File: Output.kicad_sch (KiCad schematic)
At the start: 46 parts, among them J20 Conn_01x02, J21 Conn_01x02, Q1 2N7002NXAK, Q10 2N7002NXAK, Q11 2N7002NXAK, Q2 NTR5105PT1G, Q3 NTR5105PT1G, Q4 2N7002NXAK, Q5 2N7002NXAK, Q6 2N7002NXAK, Q7 2N7002NXAK, Q8 2N7002NXAK, Q9 2N7002NXAK

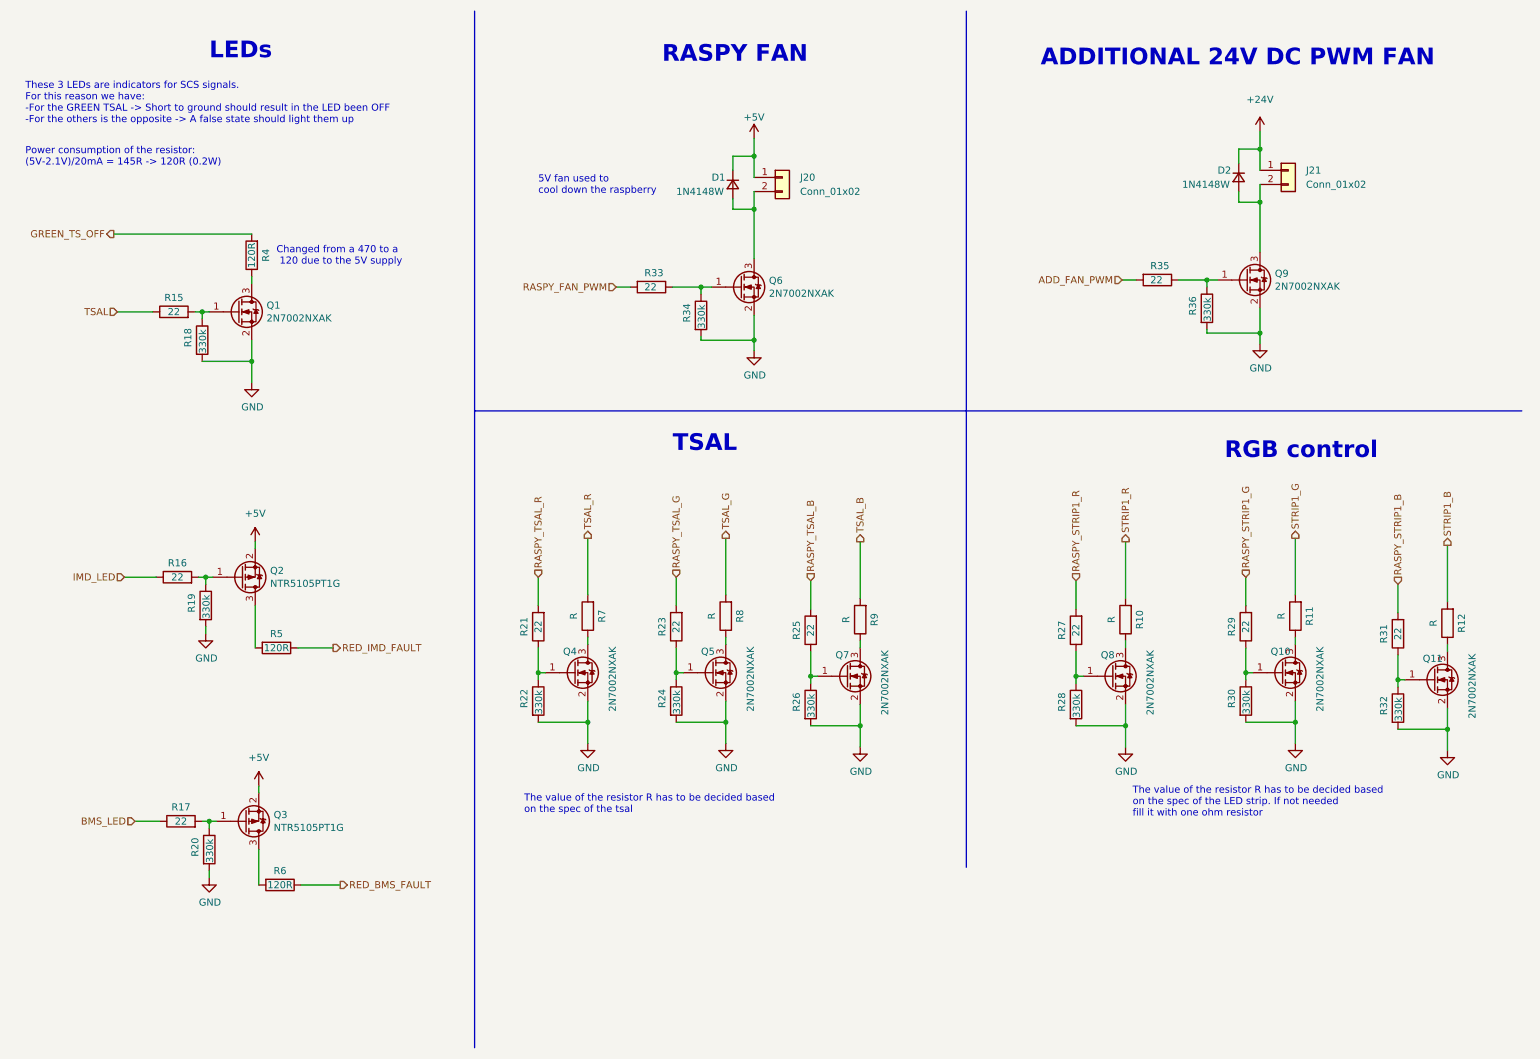
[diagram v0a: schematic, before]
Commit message: Changed mosfet, fixed all the datasheets, added 3D models
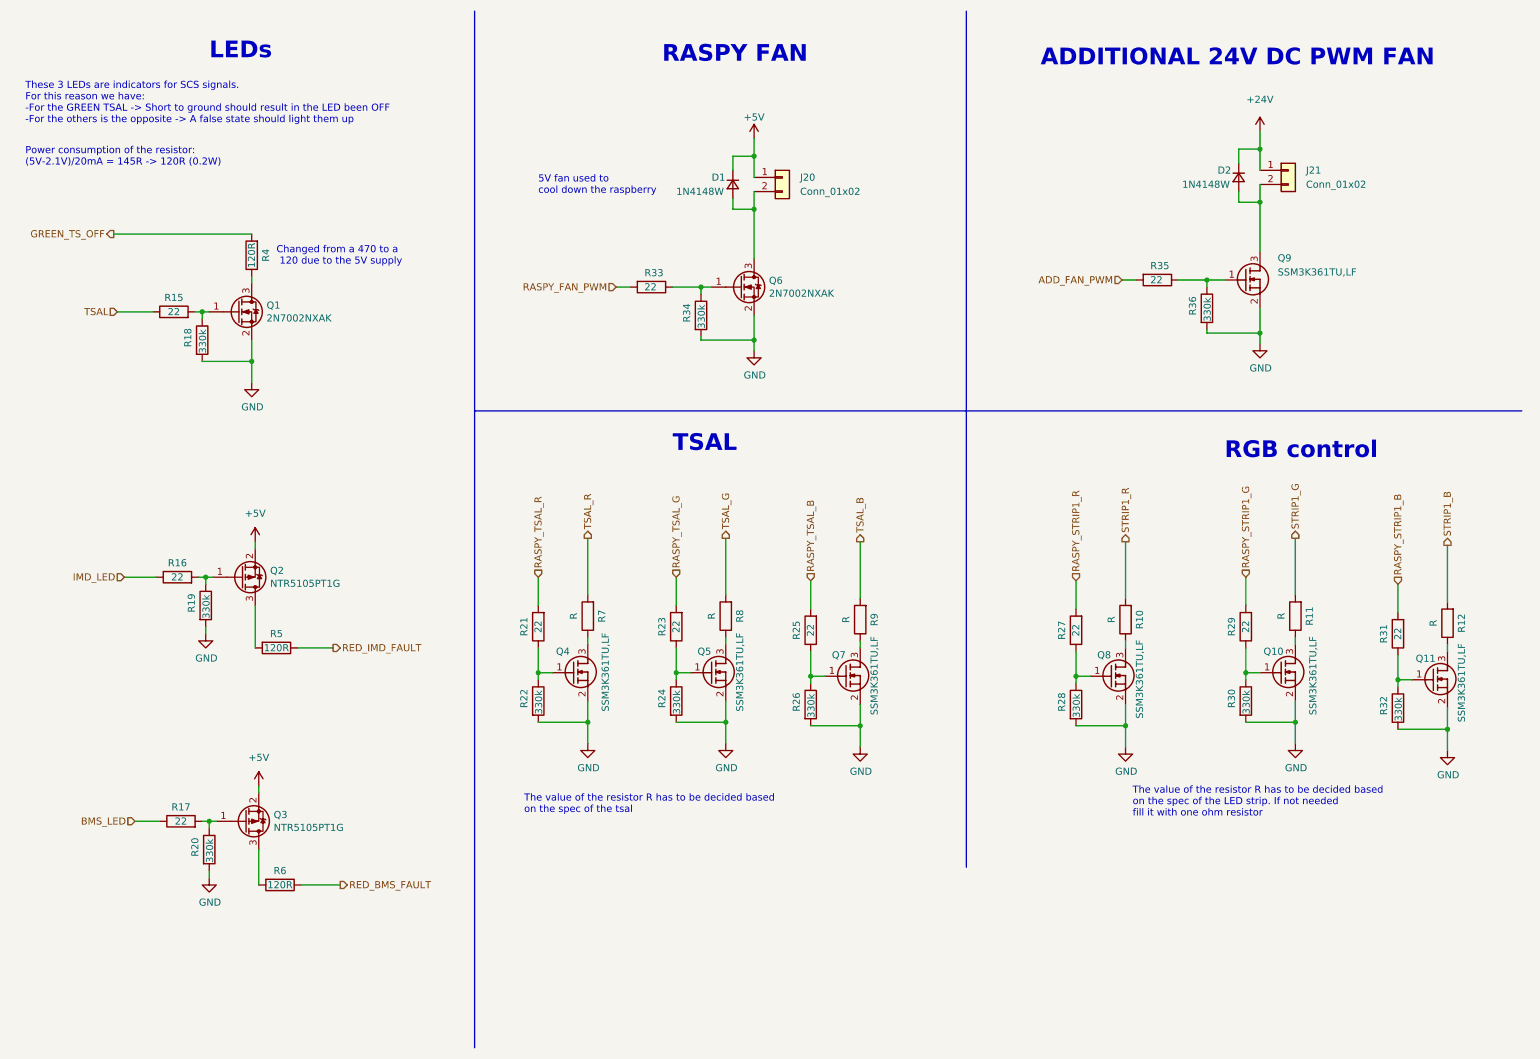
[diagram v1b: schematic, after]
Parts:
- removed Q10, Q11, Q4, Q5, Q7, Q8, Q9: 2N7002NXAK, Package_TO_SOT_SMD:SOT-23, symbol Device:Q_NMOS_GSD
- added Q10, Q11, Q4, Q5, Q7, Q8, Q9: SSM3K361TU,LF, 00_proj-lib:SOTFL65P210X75-3N, symbol 00_proj-lib:SSM3K361TU,LF
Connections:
- net GND: now also Q10.2 (S), Q11.2 (S), Q4.2 (S), Q5.2 (S), Q7.2 (S), Q8.2 (S), Q9.2 (S)
- net at R27.1, R28.1: now also Q8.1 (G)
- net at R10.1: now also Q8.3 (D)
- net at R23.1, R24.1: now also Q5.1 (G)
- net at D2.2 (A), J21.2 (Pin_2): now also Q9.3 (D)
- net at R12.1: now also Q11.3 (D)
- net at R11.1: now also Q10.3 (D)
- net at R31.1, R32.1: now also Q11.1 (G)
- net at R25.1, R26.1: now also Q7.1 (G)
- net at R35.1, R36.1: now also Q9.1 (G)
- net at R8.1: now also Q5.3 (D)
- net at R9.1: now also Q7.3 (D)
- net at R29.1, R30.1: now also Q10.1 (G)
- net at R21.1, R22.1: now also Q4.1 (G)
- net at R7.1: now also Q4.3 (D)

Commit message: Major changes after the schematic review. Refer to Github for all the changes
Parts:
- removed D1, D2: 1N4148W, Diode_SMD:D_SOD-323_HandSoldering, symbol Device:D_Small
- removed J20: Conn_01x02, Connector_Molex:Molex_Micro-Fit_3.0_43650-0215_1x02_P3.00mm_Vertical, symbol Connector_Generic:Conn_01x02
- removed Q6: 2N7002NXAK, Package_TO_SOT_SMD:SOT-23, symbol Device:Q_NMOS_GSD
- removed Q9: SSM3K361TU,LF, 00_proj-lib:SOTFL65P210X75-3N, symbol 00_proj-lib:SSM3K361TU,LF
- removed R33, R35: 22, Resistor_SMD:R_0603_1608Metric, symbol Device:R
- removed R34, R36: 330k, Resistor_SMD:R_0603_1608Metric, symbol Device:R
- added J22: RED_IMD_FAULT, Connector_Molex:Molex_Micro-Fit_3.0_43650-0215_1x02_P3.00mm_Vertical, symbol Connector_Generic:Conn_01x02
- added J23: RED_BMS_FAULT, Connector_Molex:Molex_Micro-Fit_3.0_43650-0215_1x02_P3.00mm_Vertical, symbol Connector_Generic:Conn_01x02
- added J24: RGB_STRIP, Connector_Molex:Molex_Micro-Fit_3.0_43650-0400_1x04_P3.00mm_Horizontal, symbol Connector_Generic:Conn_01x04
- added J25: TSAL, Connector_Molex:Molex_Micro-Fit_3.0_43650-0400_1x04_P3.00mm_Horizontal, symbol Connector_Generic:Conn_01x04
- added J?: ADD_RGB_STRIP, Connector_Molex:Molex_Micro-Fit_3.0_43650-0315_1x03_P3.00mm_Vertical, symbol Connector_Generic:Conn_01x03
- added JP?: 5V_ADD_STRIP, symbol Jumper:SolderJumper_2_Open
- added JP?: 3V3_ADD_STRIP, symbol Jumper:SolderJumper_2_Open
- J21: value Conn_01x02 -> GREEN_TS_OFF
- Q10: renamed from Q7; symbol 00_proj-lib:SSM3K361TU,LF -> Device:Q_NMOS_GSD
- Q11: symbol 00_proj-lib:SSM3K361TU,LF -> Device:Q_NMOS_GSD
- Q6: renamed from Q4; symbol 00_proj-lib:SSM3K361TU,LF -> Device:Q_NMOS_GSD
- Q7: renamed from Q8; symbol 00_proj-lib:SSM3K361TU,LF -> Device:Q_NMOS_GSD
- Q8: renamed from Q10; symbol 00_proj-lib:SSM3K361TU,LF -> Device:Q_NMOS_GSD
- Q9: renamed from Q5; symbol 00_proj-lib:SSM3K361TU,LF -> Device:Q_NMOS_GSD
- R10: renamed from R16; value 22 -> 22R
- R11: renamed from R17; value 22 -> 22R
- R15: renamed from R4; footprint Resistor_SMD:R_2512_6332Metric -> Resistor_SMD:R_0603_1608Metric
- R16: renamed from R5; footprint Resistor_SMD:R_2512_6332Metric -> Resistor_SMD:R_0603_1608Metric
- R17: renamed from R6; footprint Resistor_SMD:R_2512_6332Metric -> Resistor_SMD:R_0603_1608Metric
- R18: renamed from R21; value 22 -> 22R
- R19: renamed from R27; value 22 -> 22R
- R22: renamed from R7; footprint Resistor_SMD:R_1206_3216Metric -> Resistor_SMD:R_0805_2012Metric
- R23: renamed from R10; footprint Resistor_SMD:R_1206_3216Metric -> Resistor_SMD:R_0805_2012Metric
- R24: renamed from R23; value 22 -> 22R
- R25: renamed from R29; value 22 -> 22R
- R28: renamed from R11; footprint Resistor_SMD:R_1206_3216Metric -> Resistor_SMD:R_0805_2012Metric
- R29: renamed from R8; footprint Resistor_SMD:R_1206_3216Metric -> Resistor_SMD:R_0805_2012Metric
- R30: renamed from R25; value 22 -> 22R
- R31: value 22 -> 22R
- R34: renamed from R9; footprint Resistor_SMD:R_1206_3216Metric -> Resistor_SMD:R_0805_2012Metric
- R35: renamed from R12; footprint Resistor_SMD:R_1206_3216Metric -> Resistor_SMD:R_0805_2012Metric
- R9: renamed from R15; value 22 -> 22R
- renumbered Q1 to Q3, Q2 to Q4, Q3 to Q5, R18 to R12, R19 to R13, R20 to R14, R22 to R20, R28 to R21, R24 to R26, R30 to R27, R26 to R32, R32 to R33
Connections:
- net GREEN_TS_OFF is gone; now on an unnamed net: R15.2
- net RED_BMS_FAULT is gone; now on an unnamed net: R17.1
- net RED_IMD_FAULT is gone; now on an unnamed net: R16.1
- net +24V: now also J25.1 (Pin_1); no longer J21.1 (Pin_1)
- net +5V: now also J21.1 (Pin_1), JP?.2 (B)
- net GND: now also J22.2 (Pin_2), J23.2 (Pin_2), J?.3 (Pin_3)
- net STRIP1_B: now also J24.4 (Pin_4)
- net STRIP1_G: now also J24.3 (Pin_3)
- net STRIP1_R: now also J24.2 (Pin_2)
- net TSAL_B: now also J25.4 (Pin_4)
- net TSAL_G: now also J25.3 (Pin_3)
- net TSAL_R: now also J25.2 (Pin_2)
- net at Q5.3 (D): no longer R17.2
- net at Q4.3 (D): no longer R16.2
- new net: J?.1 (Pin_1), JP?.1 (A), JP?.1 (A)
- new net: J23.1 (Pin_1), R17.2
- new net: J22.1 (Pin_1), R16.2
- new net +12V: J24.1 (Pin_1)
- new net +3V3: JP?.2 (B)
- new net ADD_RGB_STRIP: J?.2 (Pin_2)
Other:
- note added: "ADDRESSABLE LED STRIP"
- note added: "The strip have to use the WS2812 interface in order to be controlled by the raspberry"
- note removed: "5V fan used to cool down the raspberry"
- note removed: "ADDITIONAL 24V DC PWM FAN"
- note removed: "Changed from a 470 to a 120 due to the 5V supply"
- note removed: "RASPY FAN"
- moved on the sheet: Q3, Q4, Q5, R10, R11, R12, R13, R14, R15, R16, R17, R18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

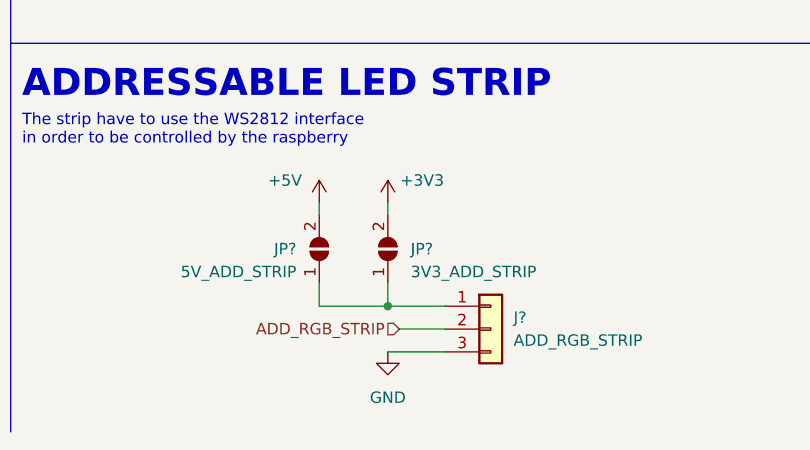
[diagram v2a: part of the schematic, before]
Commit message: modified schematic and started design pcb
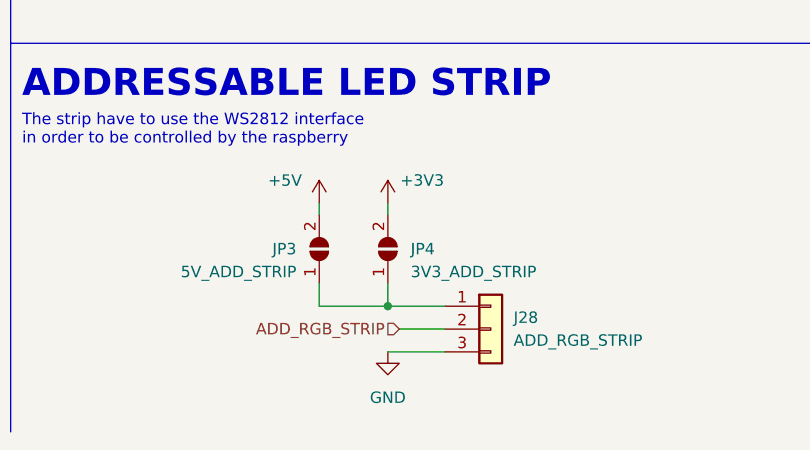
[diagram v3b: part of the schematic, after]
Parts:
- J21, J22, J23: footprint Connector_Molex:Molex_Micro-Fit_3.0_43650-0215_1x02_P3.00mm_Vertical -> Connector_Molex:Molex_Micro-Fit_3.0_43650-0200_1x02_P3.00mm_Horizontal
- JP3, JP4: renamed from JP?; footprint (none) -> Jumper:SolderJumper-2_P1.3mm_Open_RoundedPad1.0x1.5mm
- gave numbers to parts that had none: 1
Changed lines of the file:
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@@
   (symbol (lib_id "power:+5V") (at 113.03 171.45 0) (unit 1)
     (in_bom yes) (on_board yes)
-    (property "Reference" "#PWR?" (id 0) (at 113.03 175.26 0)
+    (property "Reference" "#PWR0129" (id 0) (at 113.03 175.26 0)
       (effects (font (size 1.27 1.27)) hide)
     )
@@
   (symbol (lib_id "Jumper:SolderJumper_2_Open") (at 113.03 176.53 270) (mirror x) (unit 1)
     (in_bom yes) (on_board yes)
-    (property "Reference" "JP?" (id 0) (at 110.49 176.53 90)
+    (property "Reference" "JP3" (id 0) (at 110.49 176.53 90)
       (effects (font (size 1.27 1.27)) (justify right))
     )
@@
       (effects (font (size 1.27 1.27)) (justify right))
     )
-    (property "Footprint" "" (id 2) (at 113.03 176.53 0)
+    (property "Footprint" "Jumper:SolderJumper-2_P1.3mm_Open_RoundedPad1.0x1.5mm" (id 2) (at 113.03 176.53 0)
       (effects (font (size 1.27 1.27)) hide)
     )
@@
   (symbol (lib_id "power:GND") (at 120.65 187.96 0) (unit 1)
     (in_bom yes) (on_board yes) (fields_autoplaced)
-    (property "Reference" "#PWR?" (id 0) (at 120.65 194.31 0)
+    (property "Reference" "#PWR0128" (id 0) (at 120.65 194.31 0)
       (effects (font (size 1.27 1.27)) hide)
     )
@@
   (symbol (lib_id "power:+3V3") (at 120.65 171.45 0) (unit 1)
     (in_bom yes) (on_board yes)
-    (property "Reference" "#PWR?" (id 0) (at 120.65 175.26 0)
+    (property "Reference" "#PWR0130" (id 0) (at 120.65 175.26 0)
       (effects (font (size 1.27 1.27)) hide)
     )
@@
   (symbol (lib_id "Connector_Generic:Conn_01x03") (at 132.08 185.42 0) (unit 1)
     (in_bom yes) (on_board yes) (fields_autoplaced)
-    (property "Reference" "J?" (id 0) (at 134.62 184.1499 0)
+    (property "Reference" "J28" (id 0) (at 134.62 184.1499 0)
       (effects (font (size 1.27 1.27)) (justify left))
     )
@@
     (property "Reference" "J21" (id 0) (at 67.31 48.26 0))
     (property "Value" "GREEN_TS_OFF" (id 1) (at 67.31 50.8 0))
-    (property "Footprint" "Connector_Molex:Molex_Micro-Fit_3.0_43650-0215_1x02_P3.00mm_Vertical" (id 2) (at 58.42 49.53 0)
+    (property "Footprint" "Connector_Molex:Molex_Micro-Fit_3.0_43650-0200_1x02_P3.00mm_Horizontal" (id 2) (at 58.42 49.53 0)
       (effects (font (size 1.27 1.27)) hide)
     )
@@
   (symbol (lib_id "Jumper:SolderJumper_2_Open") (at 120.65 176.53 90) (unit 1)
     (in_bom yes) (on_board yes)
-    (property "Reference" "JP?" (id 0) (at 123.19 176.53 90)
+    (property "Reference" "JP4" (id 0) (at 123.19 176.53 90)
       (effects (font (size 1.27 1.27)) (justify right))
     )
@@
       (effects (font (size 1.27 1.27)) (justify right))
     )
-    (property "Footprint" "" (id 2) (at 120.65 176.53 0)
+    (property "Footprint" "Jumper:SolderJumper-2_P1.3mm_Open_RoundedPad1.0x1.5mm" (id 2) (at 120.65 176.53 0)
       (effects (font (size 1.27 1.27)) hide)
     )
@@
     (property "Reference" "J22" (id 0) (at 67.31 123.19 0))
     (property "Value" "RED_IMD_FAULT" (id 1) (at 67.31 125.73 0))
-    (property "Footprint" "Connector_Molex:Molex_Micro-Fit_3.0_43650-0215_1x02_P3.00mm_Vertical" (id 2) (at 58.42 124.46 0)
+    (property "Footprint" "Connector_Molex:Molex_Micro-Fit_3.0_43650-0200_1x02_P3.00mm_Horizontal" (id 2) (at 58.42 124.46 0)
       (effects (font (size 1.27 1.27)) hide)
     )
@@
     (property "Reference" "J23" (id 0) (at 67.31 167.64 0))
     (property "Value" "RED_BMS_FAULT" (id 1) (at 67.31 170.18 0))
-    (property "Footprint" "Connector_Molex:Molex_Micro-Fit_3.0_43650-0215_1x02_P3.00mm_Vertical" (id 2) (at 58.42 168.91 0)
-      (effects (font (size 1.27 1.27)) hide)
-    )
+    (property "Footprint" "Connector_Molex:Molex_Micro-Fit_3.0_43650-0200_1x02_P3.00mm_Horizontal" (id 2) (at 58.42 168.91 0)
+      (effects (font (size 1.27 1.27)) hide)
+    )

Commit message: First version of the pcb layout
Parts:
- J21, J22, J23: footprint Connector_Molex:Molex_Micro-Fit_3.0_43650-0200_1x02_P3.00mm_Horizontal -> Connector_Molex:Molex_Micro-Fit_3.0_43650-0215_1x02_P3.00mm_Vertical
- J24, J25: footprint Connector_Molex:Molex_Micro-Fit_3.0_43650-0400_1x04_P3.00mm_Horizontal -> Connector_Molex:Molex_Micro-Fit_3.0_43650-0415_1x04_P3.00mm_Vertical
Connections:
- net STRIP1_B: now also J24.2 (Pin_2); no longer J24.4 (Pin_4)
- net STRIP1_R: now also J24.4 (Pin_4); no longer J24.2 (Pin_2)
- net TSAL_B: now also J25.2 (Pin_2); no longer J25.4 (Pin_4)
- net TSAL_R: now also J25.4 (Pin_4); no longer J25.2 (Pin_2)
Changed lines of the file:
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@@
     (effects (font (size 1.27 1.27)) (justify left bottom))
   )
-  (label "STRIP1_B" (at 254 132.08 0)
-    (effects (font (size 1.27 1.27)) (justify left bottom))
-  )
-  (label "TSAL_R" (at 257.81 54.61 0)
+  (label "STRIP1_R" (at 254 132.08 0)
+    (effects (font (size 1.27 1.27)) (justify left bottom))
+  )
+  (label "TSAL_B" (at 257.81 54.61 0)
     (effects (font (size 1.27 1.27)) (justify left bottom))
   )
@@
     (effects (font (size 1.27 1.27)) (justify left bottom))
   )
-  (label "STRIP1_R" (at 254 127 0)
+  (label "STRIP1_B" (at 254 127 0)
     (effects (font (size 1.27 1.27)) (justify left bottom))
   )
@@
     (effects (font (size 1.27 1.27)) (justify left bottom))
   )
-  (label "TSAL_B" (at 257.81 59.69 0)
+  (label "TSAL_R" (at 257.81 59.69 0)
     (effects (font (size 1.27 1.27)) (justify left bottom))
   )
@@
       (effects (font (size 1.27 1.27)) (justify left))
     )
-    (property "Footprint" "Connector_Molex:Molex_Micro-Fit_3.0_43650-0400_1x04_P3.00mm_Horizontal" (id 2) (at 271.78 127 0)
+    (property "Footprint" "Connector_Molex:Molex_Micro-Fit_3.0_43650-0415_1x04_P3.00mm_Vertical" (id 2) (at 271.78 127 0)
       (effects (font (size 1.27 1.27)) hide)
     )
@@
     (property "Reference" "J21" (id 0) (at 67.31 48.26 0))
     (property "Value" "GREEN_TS_OFF" (id 1) (at 67.31 50.8 0))
-    (property "Footprint" "Connector_Molex:Molex_Micro-Fit_3.0_43650-0200_1x02_P3.00mm_Horizontal" (id 2) (at 58.42 49.53 0)
+    (property "Footprint" "Connector_Molex:Molex_Micro-Fit_3.0_43650-0215_1x02_P3.00mm_Vertical" (id 2) (at 58.42 49.53 0)
       (effects (font (size 1.27 1.27)) hide)
     )
@@
       (effects (font (size 1.27 1.27)) (justify left))
     )
-    (property "Footprint" "Connector_Molex:Molex_Micro-Fit_3.0_43650-0400_1x04_P3.00mm_Horizontal" (id 2) (at 274.32 54.61 0)
+    (property "Footprint" "Connector_Molex:Molex_Micro-Fit_3.0_43650-0415_1x04_P3.00mm_Vertical" (id 2) (at 274.32 54.61 0)
       (effects (font (size 1.27 1.27)) hide)
     )
@@
     (property "Reference" "J22" (id 0) (at 67.31 123.19 0))
     (property "Value" "RED_IMD_FAULT" (id 1) (at 67.31 125.73 0))
-    (property "Footprint" "Connector_Molex:Molex_Micro-Fit_3.0_43650-0200_1x02_P3.00mm_Horizontal" (id 2) (at 58.42 124.46 0)
+    (property "Footprint" "Connector_Molex:Molex_Micro-Fit_3.0_43650-0215_1x02_P3.00mm_Vertical" (id 2) (at 58.42 124.46 0)
       (effects (font (size 1.27 1.27)) hide)
     )
@@
     (property "Reference" "J23" (id 0) (at 67.31 167.64 0))
     (property "Value" "RED_BMS_FAULT" (id 1) (at 67.31 170.18 0))
-    (property "Footprint" "Connector_Molex:Molex_Micro-Fit_3.0_43650-0200_1x02_P3.00mm_Horizontal" (id 2) (at 58.42 168.91 0)
-      (effects (font (size 1.27 1.27)) hide)
-    )
+    (property "Footprint" "Connector_Molex:Molex_Micro-Fit_3.0_43650-0215_1x02_P3.00mm_Vertical" (id 2) (at 58.42 168.91 0)
+      (effects (font (size 1.27 1.27)) hide)
+    )
